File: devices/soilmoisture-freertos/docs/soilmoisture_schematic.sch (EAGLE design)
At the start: 28 parts, among them J1 PROBE1-1FT, J2 PROBE2-3FT, J3 PROBE3-5FT, J4 PROBE4-7FT, Q1 SI2301-PFET, SW1 OTA_BTN, U1 nRF52832, U2 RFM95C-915, U3 FM25V02-8KB, U4 MCP1700-2502E, U5 W25Q16-2MB

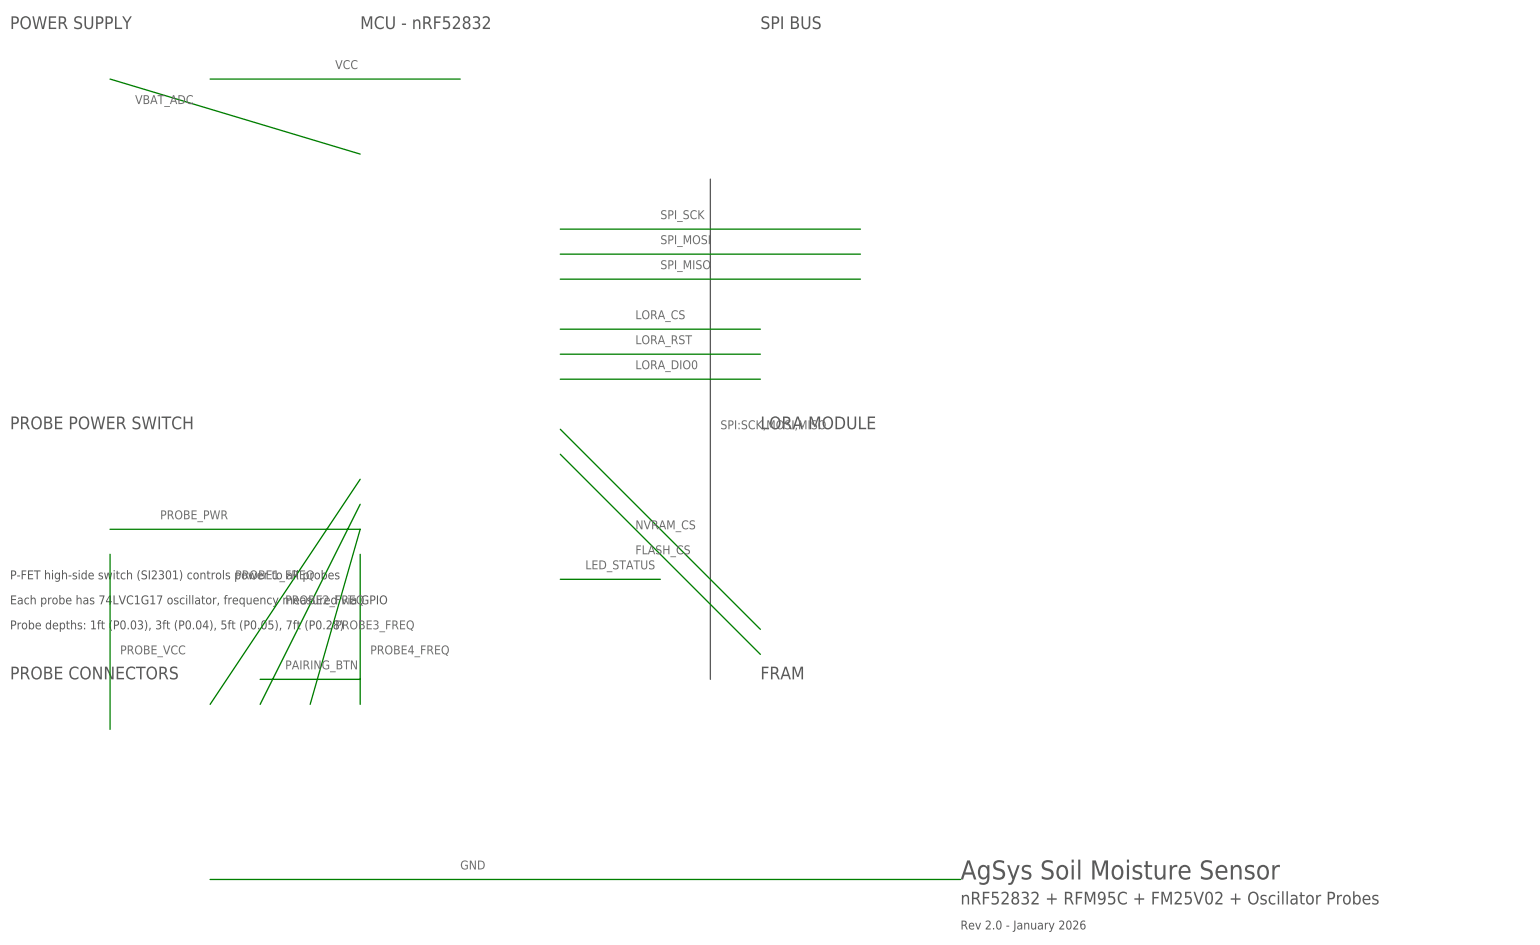
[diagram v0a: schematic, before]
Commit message: So many little fixes to schematics, to board_config.h, to OTA, to flash ram, to moving logging back to FRAM device, to looking at how to make the devices last for 10+ years, to making sure BLE is integrated correctly.
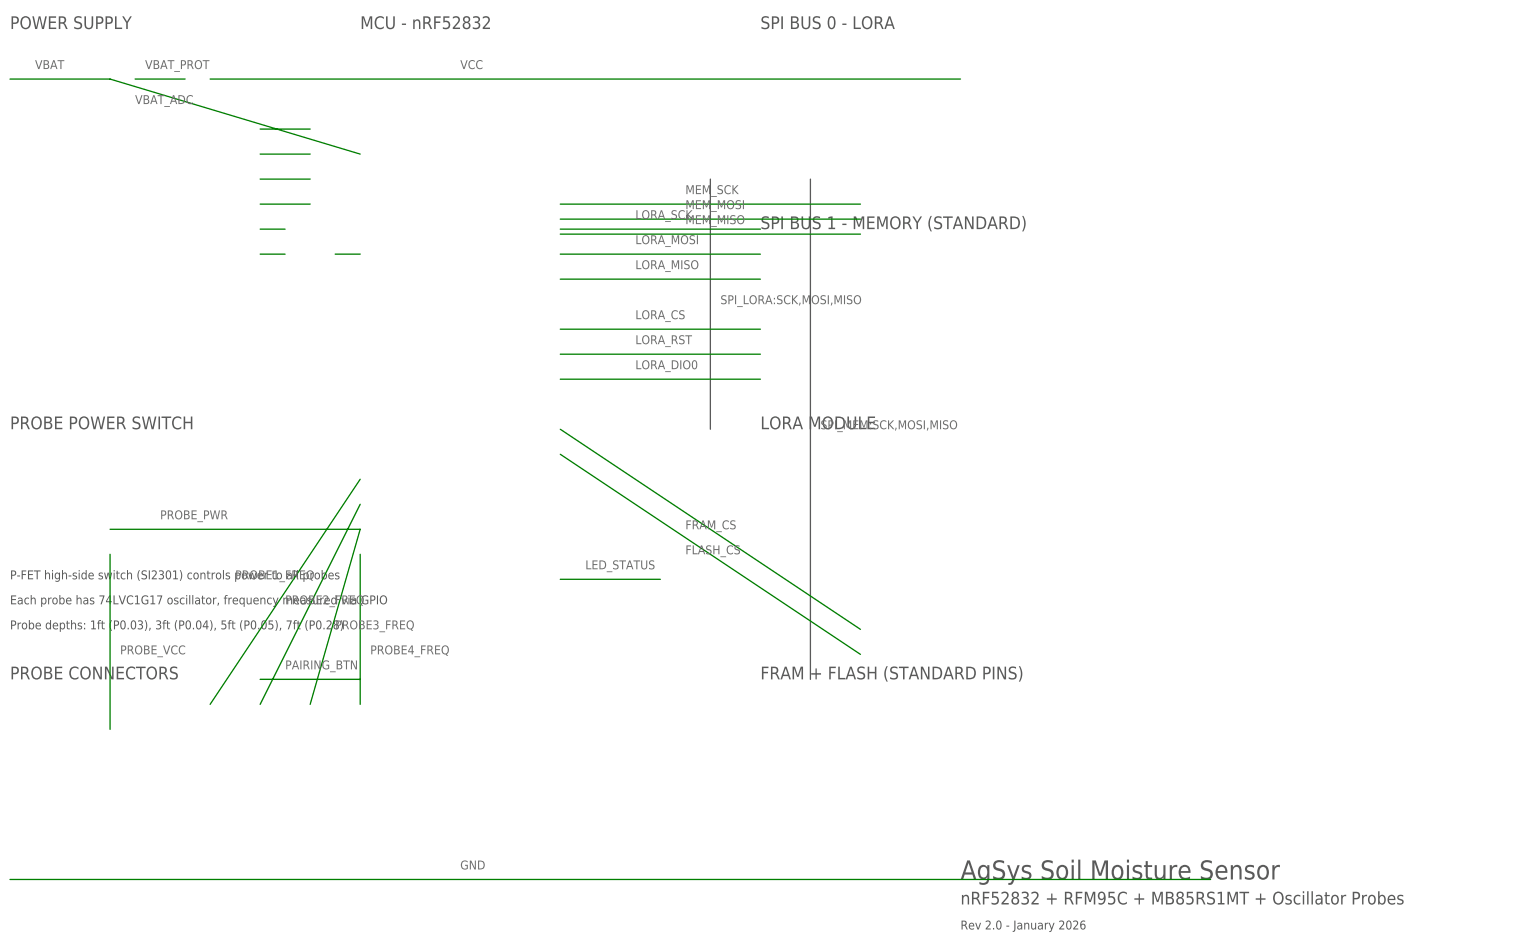
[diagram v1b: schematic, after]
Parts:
- removed R4, R5: 330, resistor:R
- added C10, C11, C13, C30, C40, C41: 100nF, capacitor:C0402
- added C12: 10uF, capacitor:C0805
- added C14: 10nF, capacitor:C0402
- added C15: 1uF, capacitor:C0402
- added C20, C21: 12pF, capacitor:C0402
- added C22, C23: 6.8pF, capacitor:C0402
- added C31: 1.5pF, capacitor:C0402
- added C32: 1.2pF, capacitor:C0402
- added D1, D2, D3, D4: PESD5V0S1BL, tvs:PESD5V0SOD323
- added J5: BATT, connector:CONN_2
- added L1: 10nH, inductor:L0402
- added L2: 5.6nH, inductor:L0402
- added Q2: SI2301CDS, mosfet:SI2301SOT23
- added R10, R11, R12, R13: 100, resistor:R0402
- added R8: 10K, resistor:R0402
- added Y1: 32MHz, crystal:CRYSTAL3215
- added Y2: 32.768kHz, crystal:CRYSTAL1610
- ANT1: value 915MHz -> 915MHz-WIRE
- C1: device capacitor:C -> capacitor:C0805
- C2: value 100nF -> 10uF; device capacitor:C -> capacitor:C0805
- C3, C4: device capacitor:C -> capacitor:C0402
- J1, J2, J3, J4: device connector:CONN_3 -> connector:JST_XH_3
- LED1: device led:LED -> led:LED0603
- Q1: value SI2301-PFET -> SI2301CDS; device mosfet:SI2301 -> mosfet:SI2301SOT23
- R1, R2: value 100K -> 1M; device resistor:R -> resistor:R0402
- R3, R6, R7: device resistor:R -> resistor:R0402
- SW1: value OTA_BTN -> PAIRING; device switch:TACTILE -> switch:TACTILE6x6
- U1: value nRF52832 -> nRF52832-QFAA; device nordic:NRF52832 -> nordic:NRF52832QFAA
- U2: value RFM95C-915 -> RFM95C-915S2
- U3: value FM25V02-8KB -> MB85RS1MTPNF; device fram:FM25V02 -> fram:MB85RS1MTSOIC8
- U4: device regulator:MCP1700 -> regulator:MCP1700SOT23
- U5: value W25Q16-2MB -> W25Q16JVSSIQ; device flash:W25Q16 -> flash:W25Q16SOIC8
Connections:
- removed net NVRAM_CS: U1.P0.11, U3.CS
- removed net SPI_MISO: U1.P0.23, U2.MISO, U3.SO
- removed net SPI_MOSI: U1.P0.24, U2.MOSI, U3.SI
- removed net SPI_SCK: U1.P0.25, U2.SCK, U3.SCK
- new net DCC: L1.1, U1.DCC
- new net DCCH: C15.1, L1.2
- new net DEC1: C14.1, U1.DEC1
- new net FRAM_CS: U1.P0.23, U3.CS
- new net LORA_MISO: U1.P0.12, U2.MISO
- new net LORA_MOSI: U1.P0.13, U2.MOSI
- new net LORA_SCK: U1.P0.14, U2.SCK
- new net MEM_MISO: U1.P0.24, U3.SO, U5.SO
- new net MEM_MOSI: U1.P0.25, U3.SI, U5.SI
- new net MEM_SCK: U1.P0.26, U3.SCK, U5.SCK
- new net VBAT: BT1.+, J5.1, Q2.S, R1.1
- new net VBAT_PROT: C1.1, Q1.S, Q2.D, U4.VIN
- new net XC1: C20.1, U1.XC1, Y1.1
- new net XC2: C21.1, U1.XC2, Y1.2
- new net XL1: C22.1, U1.XL1, Y2.1
- new net XL2: C23.1, U1.XL2, Y2.2
- net FLASH_CS: now also U1.P0.22; no longer U1.P0.12
- net GND: now also BT1.-, C1.2, C10.2, C11.2, C12.2, C2.2, C20.2, C21.2, C22.2, C23.2, C3.2, C30.2, C40.2, C41.2, D1.K, D2.K, D3.K, D4.K, J1.2, J2.2, J3.2, J4.2, J5.2, LED1.K, R2.2, R8.2, SW1.2, U5.GND
- net LORA_CS: now also U1.P0.11; no longer U1.P0.27
- net VCC: now also C10.1, C11.1, C12.1, C13.1, C2.1, C30.1, C40.1, C41.1, R6.1, R7.1, U4.VOUT, U5.VCC
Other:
- note added: "FRAM + FLASH (STANDARD PINS)"
- note added: "SPI BUS 0 - LORA"
- note added: "SPI BUS 1 - MEMORY (STANDARD)"
- note added: "nRF52832 + RFM95C + MB85RS1MT + Oscillator Probes"
- note removed: "FRAM"
- note removed: "SPI BUS"
- note removed: "nRF52832 + RFM95C + FM25V02 + Oscillator Probes"

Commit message: renamed valve actuator directory to match the type valve support.  Added solenoid valve actuator
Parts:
- U4: value MCP1700-2502E -> TPS7A0225PDBVR; device regulator:MCP1700SOT23 -> regulator:AP2112KSOT23-5
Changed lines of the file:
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@@
 <part name="C41" library="capacitor" deviceset="C" device="0402" value="100nF"/>
 <!-- ================================================================== -->
-<!-- POWER SUPPLY - LDO (3.0-4.2V to 2.5V) -->
+<!-- POWER SUPPLY - LDO (3.0-4.2V to 2.5V, TPS7A02 25nA Iq) -->
 <!-- ================================================================== -->
-<part name="U4" library="regulator" deviceset="MCP1700" device="SOT23" value="MCP1700-2502E"/>
+<part name="U4" library="regulator" deviceset="AP2112K" device="SOT23-5" value="TPS7A0225PDBVR"/>
 <part name="C1" library="capacitor" deviceset="C" device="0805" value="10uF"/>
 <part name="C2" library="capacitor" deviceset="C" device="0805" value="10uF"/>
